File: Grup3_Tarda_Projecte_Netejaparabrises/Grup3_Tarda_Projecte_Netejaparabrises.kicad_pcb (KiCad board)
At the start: 4 copper layers, 162.4 x 126.5 mm, 97 parts, among them IC1 L78S05CV, IC2 PIC18F258-I_SO, J1 Screw_Terminal_01x02, J10 Screw_Terminal_01x02, J11 Screw_Terminal_01x02, J12 Screw_Terminal_01x02, J13 FINAL DE CARRERA, J14 FINAL DE CARRERA, J2 BOTONERA, J3 PROGRAMMING CON, J4 JP1, J5 DE9_Plug_MountingHoles, J6 DE9_Plug_MountingHoles, J7 CONEXIOSENSOR, J8 Screw_Terminal_01x02, J9 Screw_Terminal_01x02, K1 1393280-6, K2 1393280-6, K3 1393280-6, K4 1393280-6, K5 1393280-6, K6 1393280-6, K7 1393280-6, K8 1393280-6, K9 1393280-6, Q1 BC817-25_RF, Q2 BC817-25_RF, Q3 BC817-25_RF, Q4 BC817-25_RF, Q5 BC817-25_RF, Q6 BC817-25_RF, Q7 BC817-25_RF, U1 Value, U2 LM393, Y1 ABLS2-8.000MHZ-D4Y-T

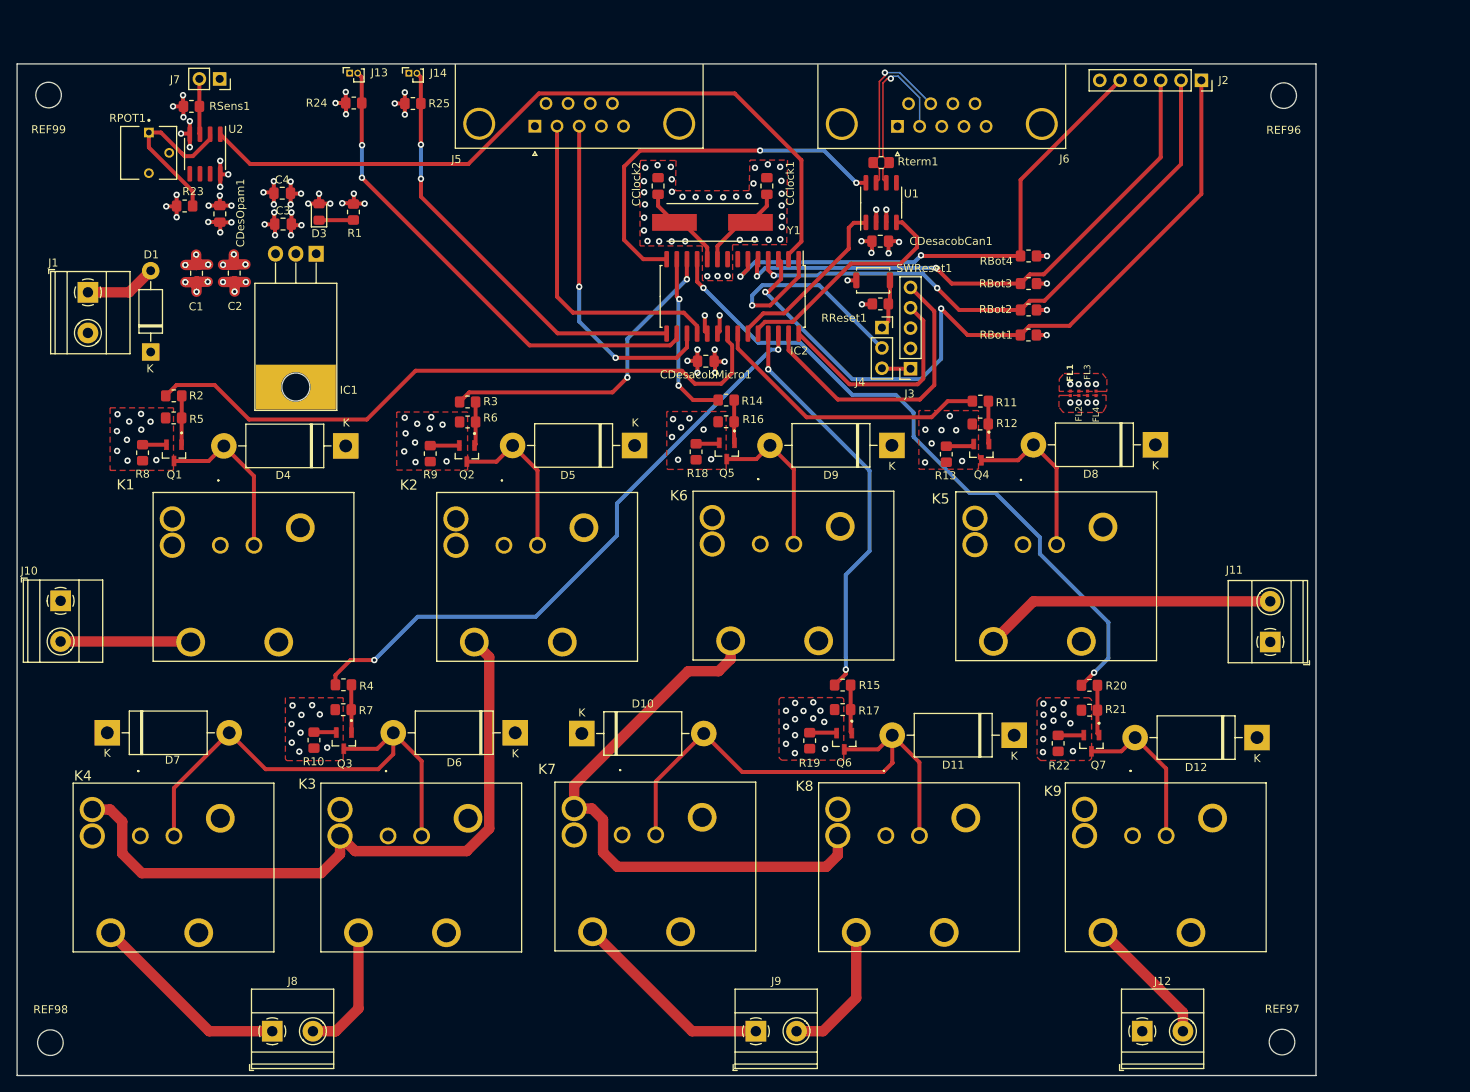
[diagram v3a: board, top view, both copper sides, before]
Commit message: canvi de posicio de ferrites i connectors reset debug
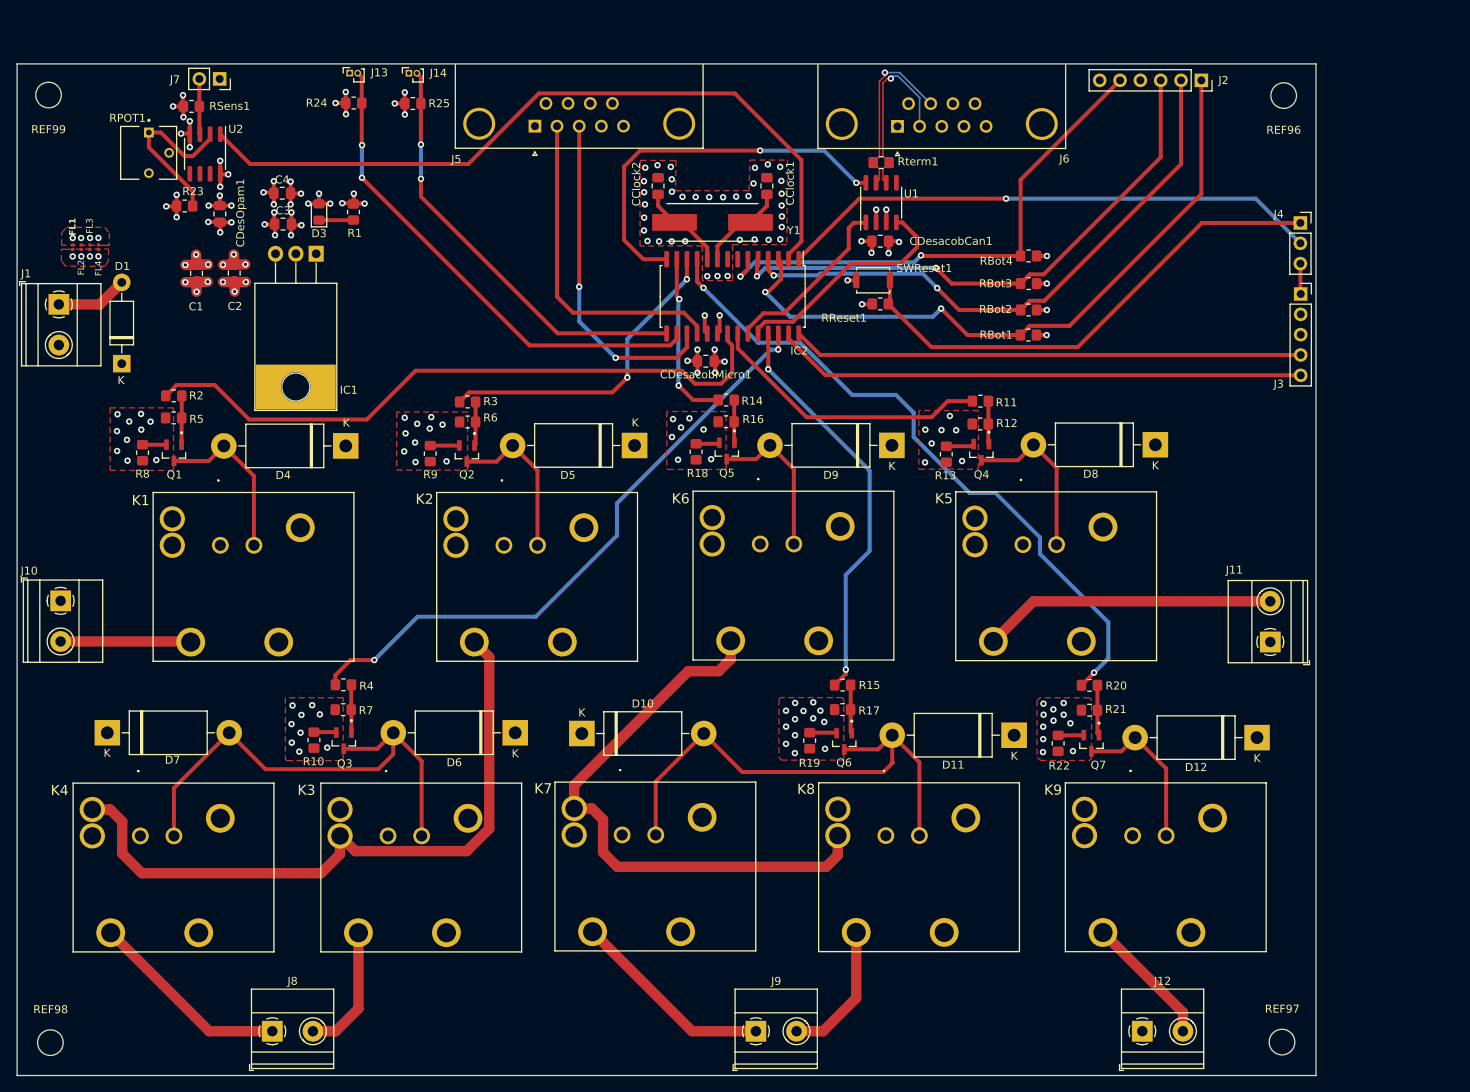
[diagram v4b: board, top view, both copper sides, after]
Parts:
- moved FL2 126.0 mm to (61.4, 55.6)
- moved FL1 126.0 mm to (60.3, 55.6)
- moved FL3 126.0 mm to (62.5, 55.6)
- moved FL4 126.0 mm to (63.5, 55.6)
- moved J4 53.9 mm to (213.8, 52.6)
- moved J3 49.7 mm to (213.8, 61.5), turned to 0 degrees
- moved J1 3.94 mm to (58.6, 62.8)
- moved D1 3.90 mm to (66.4, 70.2)
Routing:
- net /Digital/Vsw: track 6.32 -> 63.2 mm
- net /Digital/MCLR: track 30.7 -> 68.2 mm
- net PGD: track 28.0 -> 63.9 mm
- net PGC: track 37.0 -> 66.5 mm
- net /Digital/Vboto1: track 94.5 -> 84.4 mm

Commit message: Fitxer BOM
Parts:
- R1: value 220 -> 220R

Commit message: definitiu
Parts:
- J13, J14: footprint Connector_PinSocket_1.00mm:PinSocket_1x02_P1.00mm_Vertical -> Connector_PinHeader_2.54mm:PinHeader_1x02_P2.54mm_Vertical
- J2: footprint Connector_PinSocket_2.54mm:PinSocket_1x06_P2.54mm_Vertical -> Connector_PinHeader_2.54mm:PinHeader_1x06_P2.54mm_Vertical
- J3: footprint Connector_PinSocket_2.54mm:PinSocket_1x05_P2.54mm_Vertical -> Connector_PinHeader_2.54mm:PinHeader_1x05_P2.54mm_Vertical
- J4: footprint Connector_PinSocket_2.54mm:PinSocket_1x03_P2.54mm_Vertical -> Connector_PinHeader_2.54mm:PinHeader_1x03_P2.54mm_Vertical
- J7: footprint Connector_PinSocket_2.54mm:PinSocket_1x02_P2.54mm_Vertical -> Connector_PinHeader_2.54mm:PinHeader_1x02_P2.54mm_Vertical
- moved J14 1.33 mm to (101.2, 34.6)
- moved J13 1.29 mm to (93.9, 34.6)
- moved R25 0.67 mm to (102.8, 38.4)
- moved R24 0.63 mm to (95.4, 38.2)
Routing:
- net /Digital/Vfin_back: track 53.4 -> 52.6 mm
- net /Digital/Vfin_front: track 62.4 -> 61.5 mm
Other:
- board text added: "AIDAR IGLESIAS DAVID MIRAVENT BIEL HORNAS PROJECTE NETEJA-PARABRISES"
